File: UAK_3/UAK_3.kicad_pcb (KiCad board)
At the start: 2 copper layers, 100 x 90 mm, 63 parts, among them K1 Кнопка_FSMSM, K2 Кнопка_FSMSM, X1 Крепежное_отверстие_М3, X2 Крепежное_отверстие_М3, X3 Крепежное_отверстие_М3, X4 Крепежное_отверстие_М3

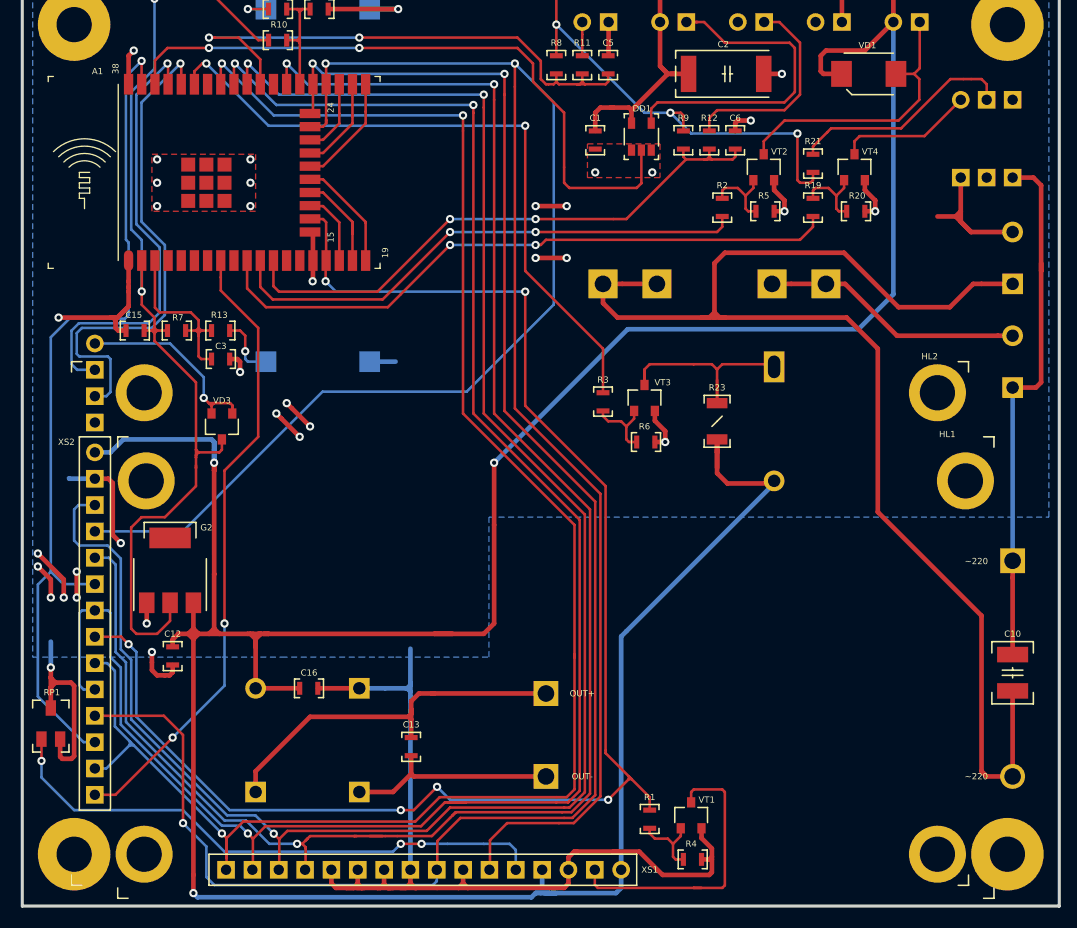
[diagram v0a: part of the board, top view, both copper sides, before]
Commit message: добавлены сопротивления: в управление ЖК и выход 220
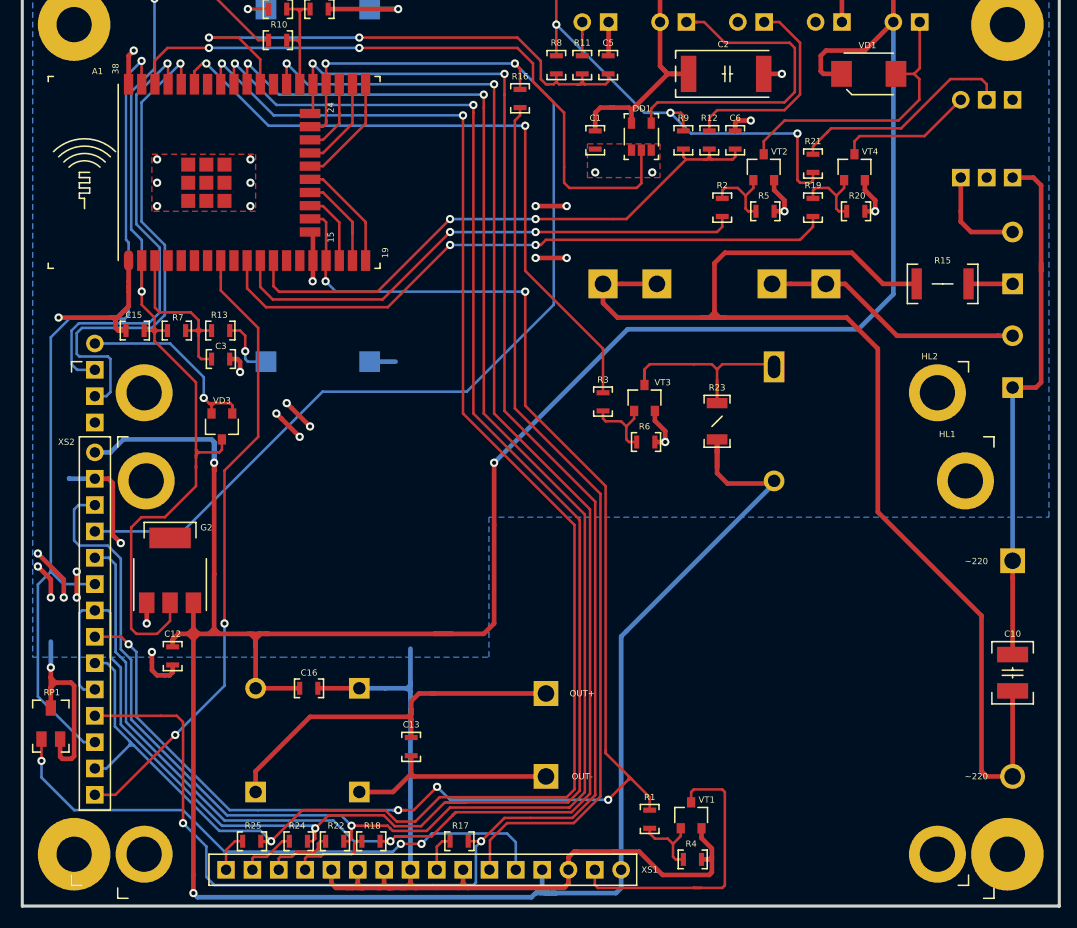
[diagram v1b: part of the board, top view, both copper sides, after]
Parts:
- added R15: Резистор_0,5Вт, N_RLC:Резистор_SMD_2010-0,5_Вт, F.Cu at (161.2, 80.0)
- added R16: Резистор_0,065Вт, N_RLC:Резистор_SMD_0603_0,065_Вт, F.Cu at (123.0, 63.0)
- added R17: Резистор_0,065Вт, N_RLC:Резистор_SMD_0603_0,065_Вт, F.Cu at (116.2, 133.8)
- added R18: Резистор_0,065Вт, N_RLC:Резистор_SMD_0603_0,065_Вт, F.Cu at (107.8, 133.8)
- added R22: Резистор_0,065Вт, N_RLC:Резистор_SMD_0603_0,065_Вт, F.Cu at (104.2, 133.8)
- added R24: Резистор_0,065Вт, N_RLC:Резистор_SMD_0603_0,065_Вт, F.Cu at (100.8, 133.8)
- added R25: Резистор_0,065Вт, N_RLC:Резистор_SMD_0603_0,065_Вт, F.Cu at (96.2, 133.8)
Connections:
- HL1 pad 11: /LCD_DATA_4 -> Net-(HL1-Pad11)
- HL1 pad 12: /LCD_DATA_5 -> Net-(HL1-Pad12)
- HL1 pad 13: /LCD_DATA_6 -> Net-(HL1-Pad13)
- HL1 pad 14: /LCD_DATA_7 -> Net-(HL1-Pad14)
- HL1 pad 4: /LCD_A0 -> Net-(HL1-Pad4)
- HL1 pad 6: /LCD_E -> Net-(HL1-Pad6)
- XT8 pad 2: /220_L_FU -> /220_L_OUT
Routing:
- net /LCD_A0: track 193.4 -> 106.8 mm
- net Net-(HL1-Pad4): track 0.00 -> 85.3 mm
- net /220_L_FU: track 131.9 -> 120.8 mm
- net Net-(HL1-Pad11): track 0.00 -> 7.70 mm
- net Net-(HL1-Pad12): track 0.00 -> 6.60 mm
- net Net-(HL1-Pad13): track 0.00 -> 5.34 mm
- net /220_N_OUT: track 14.2 -> 9.66 mm
- net /220_L_OUT: track 0.00 -> 4.25 mm
- net Net-(HL1-Pad14): track 0.00 -> 3.85 mm
- net Net-(HL1-Pad6): track 0.00 -> 3.72 mm
- net /LCD_DATA_4: track 169.3 -> 167.0 mm
- net /LCD_E: track 164.5 -> 166.3 mm, vias 3 -> 4
- net /LCD_DATA_5: track 177.0 -> 175.5 mm
- net Net-(HL1-Pad3): track 54.9 -> 56.1 mm
- net /LCD_LED: track 146.9 -> 148.1 mm
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
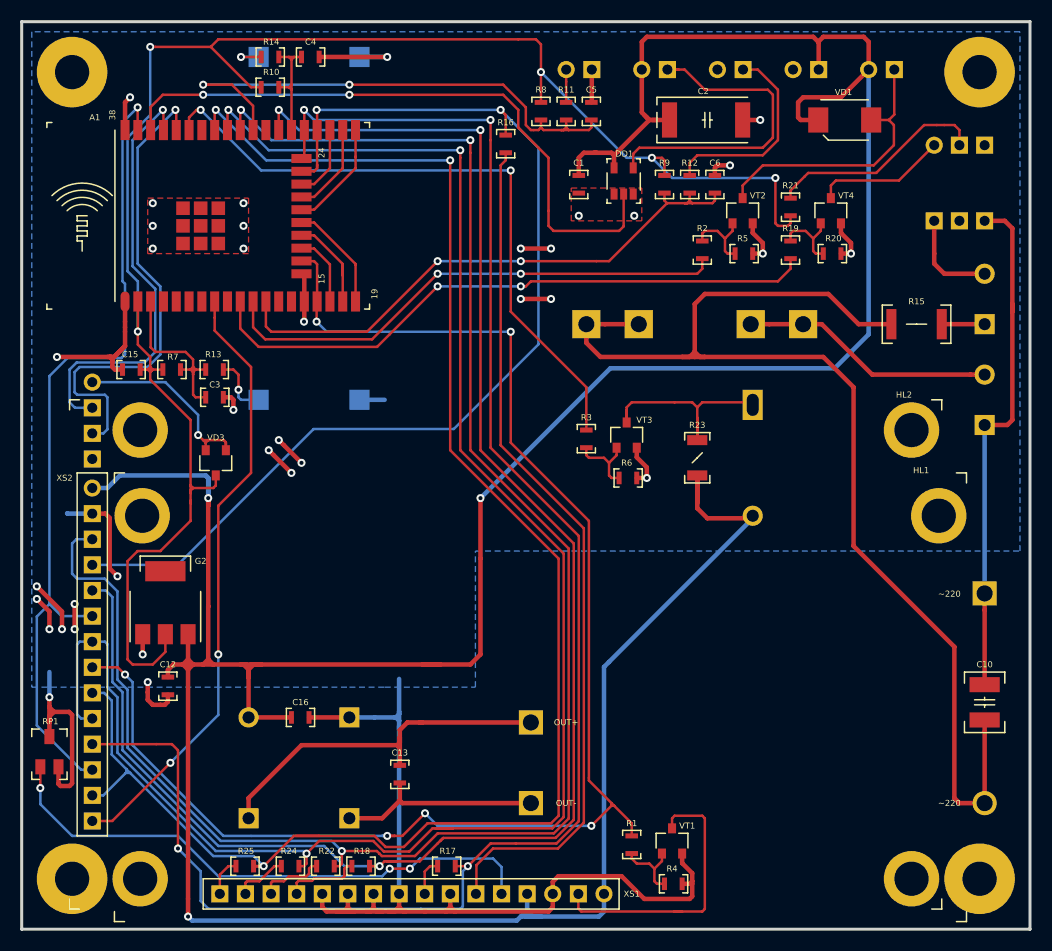
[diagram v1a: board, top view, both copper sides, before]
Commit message: заменены клеммники
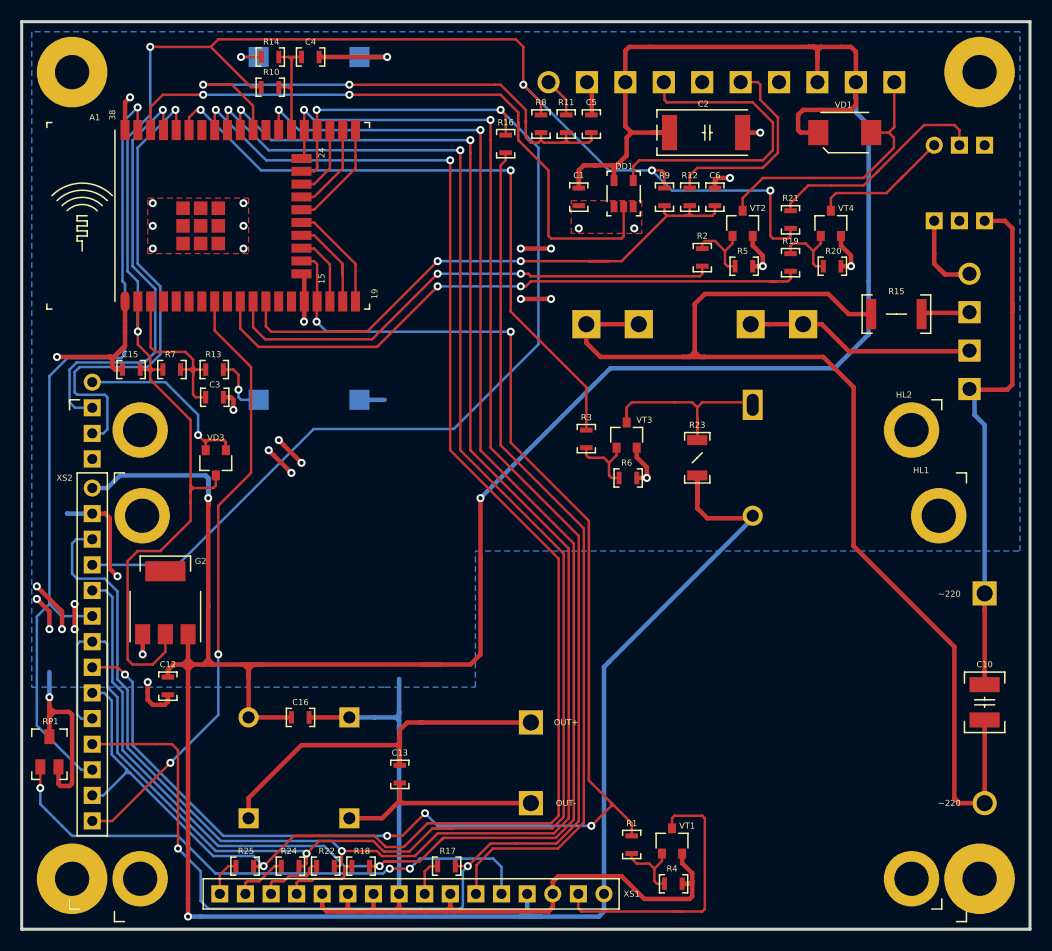
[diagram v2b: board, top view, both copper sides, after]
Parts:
- removed XT1, XT2, XT3, XT6, XT7: Клеммник_х2_308-021-14, N_X:Клеммник_х2_шаг2.54
- removed XT4, XT8: Клеммник_х2_KLS2-300-5.00-02P-2S, N_X:Клеммник_х2_шаг5
- added X5: Клеммник_х4, N_X:Клеммник_х4_шаг3,81_15EDGRC, B.Cu at (169.0, 75.0)
- added X6: Клеммник_х10, N_X:Клеммник_х10_шаг3,81_15EDGRC, B.Cu at (127.2, 56.0)
- moved D1 6.49 mm to (107.5, 66.8)
- moved R15 2.24 mm to (159.2, 79.0)
- moved C1 1.25 mm to (130.2, 66.5)
- moved C2 1.25 mm to (139.2, 61.0)
- moved C5 1.25 mm to (131.5, 59.2)
- moved C6 1.25 mm to (143.8, 66.5)
- moved DD1 1.25 mm to (133.8, 68.3)
- moved R11 1.25 mm to (129.0, 59.2)
- moved R12 1.25 mm to (141.2, 66.5)
- moved R19 1.25 mm to (151.2, 73.0)
- moved R20 1.25 mm to (154.5, 74.2)
- moved R21 1.25 mm to (151.2, 68.8)
- moved R5 1.25 mm to (145.8, 74.2)
- moved R8 1.25 mm to (126.5, 59.2)
- moved R9 1.25 mm to (138.8, 66.5)
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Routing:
- net /5V: track 367.5 -> 372.1 mm
- net /220_L_FU: track 120.8 -> 118.4 mm
- net /220_L: track 25.3 -> 23.3 mm
- net /3V3: track 174.1 -> 175.9 mm
- net /EXT_BUTTON: track 56.2 -> 57.6 mm
- net /220_N_OUT: track 9.66 -> 11.1 mm
- net /DOOR_SENSOR: track 53.1 -> 54.5 mm
- net /220_N: track 51.5 -> 52.7 mm
- net /220_L_OUT: track 4.25 -> 5.30 mm
- net Net-(DA1-Pad1): track 13.2 -> 14.2 mm
- net /LED_WS2812: track 63.7 -> 64.6 mm
- net Net-(DA1-Pad2): track 21.9 -> 22.8 mm
- net /DOOR_1: track 3.25 -> 3.97 mm
- net /LED_OUT: track 32.8 -> 32.1 mm
- net /D_OUT_1: track 27.6 -> 27.0 mm
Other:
- board text added: "BUTT LED"
- board text added: "EXT BUTTON"
- board text added: "LED WS2812"
- board text removed: "12V OUT"
- board text removed: "5V_OUT"
- board text removed: "BUTT_LED"
- board text removed: "EXT_BUTTON"
- board text removed: "LED_WS2812"

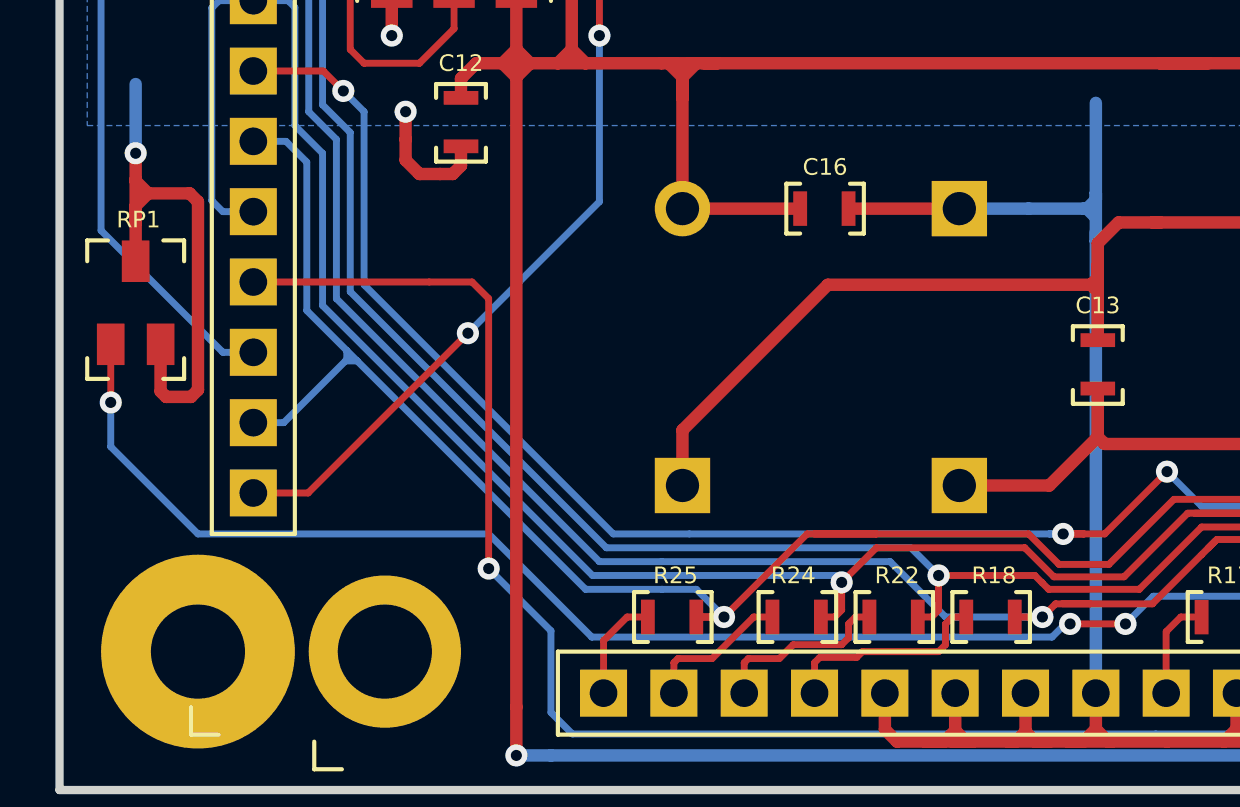
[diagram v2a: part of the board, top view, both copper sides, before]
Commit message: заменен потенциометр, начал формировать BOM
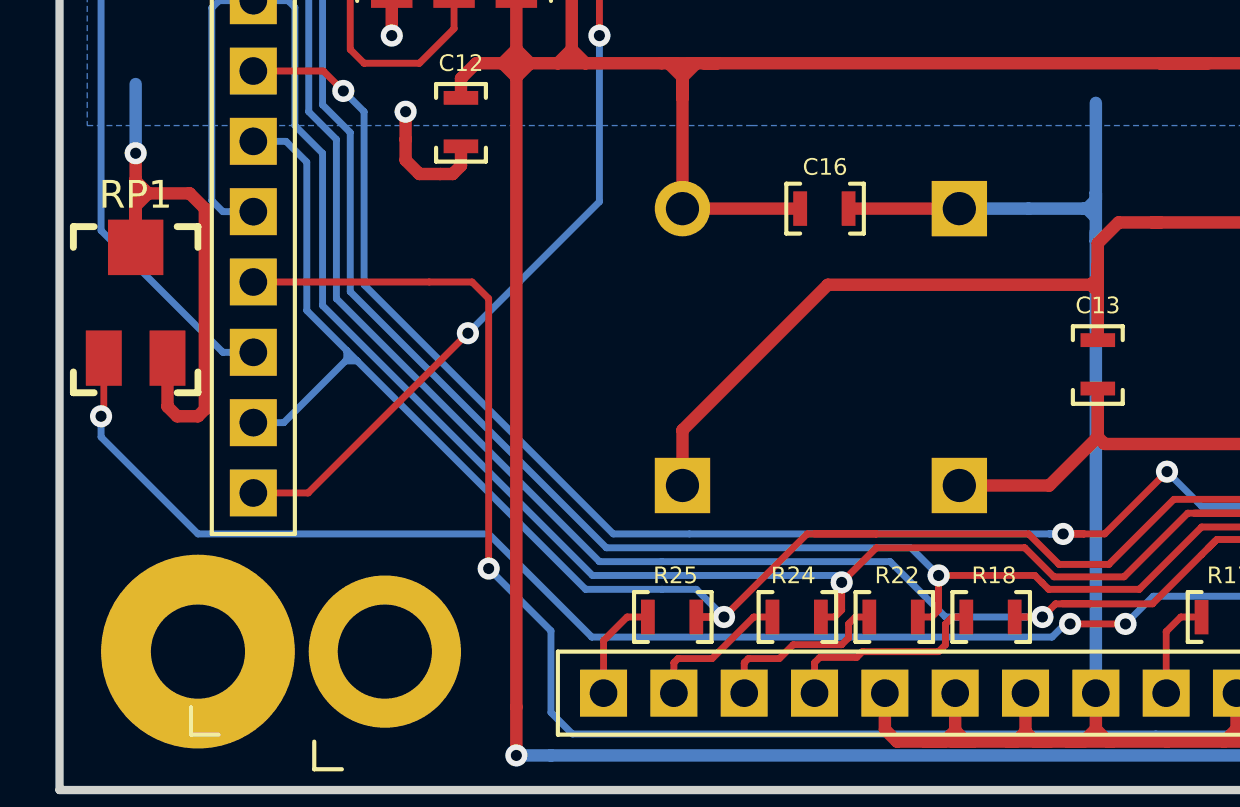
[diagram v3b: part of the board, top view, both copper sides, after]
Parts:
- RP1: footprint MOTOR_IMPORT_OTK:резистор_подстроечный_PVZ3A334 -> N_RLC:резистор_подстроечный_3314J-1
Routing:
- net /GND: track 214.0 -> 216.4 mm

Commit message: подготовлены файлы для заказа в JLCPCB
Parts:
- removed the R9 at (138.8, 66.5)
- added R20: Резистор_0,065Вт, N_RLC:Резистор_SMD_0603_0,065_Вт_pnp, F.Cu at (63.8, -72.6)
- A1: footprint N_A:ESP32_WROVER_or_WROOM32 -> N_A:ESP32_WROVER_or_WROOM32_pnp
- C1, C3, C4, C5, C6: footprint N_RLC:Конденсатор_SMD_0603 -> N_RLC:Конденсатор_SMD_0603_pnp
- C10: renamed from C13; footprint N_RLC:Конденсатор_SMD_0603 -> N_RLC:Конденсатор_SMD_0603_pnp
- C11: renamed from C16; footprint N_RLC:Конденсатор_SMD_0603 -> N_RLC:Конденсатор_SMD_0603_pnp
- C2: footprint MOTOR_RLC:Конденсатор_тантал_SMD_m7343 -> N_RLC:Конденсатор_тантал_SMD_m7343_pnp
- C7: renamed from C10; footprint N_RLC:Конденсатор_SMD_1210 -> N_RLC:Конденсатор_SMD_1210_pnp
- C8: renamed from C12; footprint N_RLC:Конденсатор_SMD_0603 -> N_RLC:Конденсатор_SMD_0603_pnp
- C9: renamed from C15; footprint N_RLC:Конденсатор_SMD_0603 -> N_RLC:Конденсатор_SMD_0603_pnp
- DD1: footprint N_G:Преобразователь_LM2703_SOT-23-5 -> N_G:SOT-23-5_pnp
- G2: footprint N_VD_HL:Транзистор_NPN_SOT223 -> N_VD_HL:Транзистор_NPN_SOT223_pnp
- R1: renamed from R19; footprint N_RLC:Резистор_SMD_0603_0,065_Вт -> N_RLC:Резистор_SMD_0603_0,065_Вт_pnp
- R10: renamed from R25; footprint N_RLC:Резистор_SMD_0603_0,065_Вт -> N_RLC:Резистор_SMD_0603_0,065_Вт_pnp
- R11: renamed from R1; footprint N_RLC:Резистор_SMD_0603_0,065_Вт -> N_RLC:Резистор_SMD_0603_0,065_Вт_pnp
- R12: renamed from R2; footprint N_RLC:Резистор_SMD_0603_0,065_Вт -> N_RLC:Резистор_SMD_0603_0,065_Вт_pnp
- R13: renamed from R3; footprint N_RLC:Резистор_SMD_0603_0,065_Вт -> N_RLC:Резистор_SMD_0603_0,065_Вт_pnp
- R14: renamed from R4; footprint N_RLC:Резистор_SMD_0603_0,065_Вт -> N_RLC:Резистор_SMD_0603_0,065_Вт_pnp
- R15: renamed from R5; footprint N_RLC:Резистор_SMD_0603_0,065_Вт -> N_RLC:Резистор_SMD_0603_0,065_Вт_pnp
- R16: renamed from R6; footprint N_RLC:Резистор_SMD_0603_0,065_Вт -> N_RLC:Резистор_SMD_0603_0,065_Вт_pnp
- R17: renamed from R23; footprint N_RLC:Резистор_SMD_1206-0,25_Вт -> N_RLC:Резистор_SMD_1206-0,25_Вт_pnp
- R18: renamed from R7; footprint N_RLC:Резистор_SMD_0603_0,065_Вт -> N_RLC:Резистор_SMD_0603_0,065_Вт_pnp
- R19: renamed from R8; footprint N_RLC:Резистор_SMD_0603_0,065_Вт -> N_RLC:Резистор_SMD_0603_0,065_Вт_pnp
- R2: renamed from R20; footprint N_RLC:Резистор_SMD_0603_0,065_Вт -> N_RLC:Резистор_SMD_0603_0,065_Вт_pnp
- R21: renamed from R10; footprint N_RLC:Резистор_SMD_0603_0,065_Вт -> N_RLC:Резистор_SMD_0603_0,065_Вт_pnp
- R22: renamed from R11; footprint N_RLC:Резистор_SMD_0603_0,065_Вт -> N_RLC:Резистор_SMD_0603_0,065_Вт_pnp
- R23: renamed from R12; footprint N_RLC:Резистор_SMD_0603_0,065_Вт -> N_RLC:Резистор_SMD_0603_0,065_Вт_pnp
- R24: renamed from R13; footprint N_RLC:Резистор_SMD_0603_0,065_Вт -> N_RLC:Резистор_SMD_0603_0,065_Вт_pnp
- R25: renamed from R14; footprint N_RLC:Резистор_SMD_0603_0,065_Вт -> N_RLC:Резистор_SMD_0603_0,065_Вт_pnp
- R3: renamed from R21; footprint N_RLC:Резистор_SMD_0603_0,065_Вт -> N_RLC:Резистор_SMD_0603_0,065_Вт_pnp
- R4: renamed from R15; footprint N_RLC:Резистор_SMD_2010-0,5_Вт -> N_RLC:Резистор_SMD_2010-0,5_Вт_pnp
- R5: renamed from R16; footprint N_RLC:Резистор_SMD_0603_0,065_Вт -> N_RLC:Резистор_SMD_0603_0,065_Вт_pnp
- R6: renamed from R17; footprint N_RLC:Резистор_SMD_0603_0,065_Вт -> N_RLC:Резистор_SMD_0603_0,065_Вт_pnp
- R7: renamed from R18; footprint N_RLC:Резистор_SMD_0603_0,065_Вт -> N_RLC:Резистор_SMD_0603_0,065_Вт_pnp
- R8: renamed from R22; footprint N_RLC:Резистор_SMD_0603_0,065_Вт -> N_RLC:Резистор_SMD_0603_0,065_Вт_pnp
- R9: renamed from R24; footprint N_RLC:Резистор_SMD_0603_0,065_Вт -> N_RLC:Резистор_SMD_0603_0,065_Вт_pnp
- RP1: footprint N_RLC:резистор_подстроечный_3314J-1 -> N_RLC:резистор_подстроечный_3314J-1_pnp
- VD1: footprint N_VD_HL:Диод_SMB -> N_VD_HL:Диод_SMB_pnp
- VD2: renamed from VD3; footprint MOTOR_VD_VT_HL:Корпус_КТ-46 -> N_DD:Корпус_КТ-46_pnp
- VT1: renamed from VT4; footprint MOTOR_VD_VT_HL:Корпус_КТ-46 -> N_DD:Корпус_КТ-46_pnp
- VT2: renamed from VT1; footprint MOTOR_VD_VT_HL:Корпус_КТ-46 -> N_DD:Корпус_КТ-46_pnp
- VT3: renamed from VT2; footprint MOTOR_VD_VT_HL:Корпус_КТ-46 -> N_DD:Корпус_КТ-46_pnp
- VT4: renamed from VT3; footprint MOTOR_VD_VT_HL:Корпус_КТ-46 -> N_DD:Корпус_КТ-46_pnp
- moved A1 162.5 mm to (19.2, -70.8)
- moved C7 160.4 mm to (95.5, -22.5)
- moved R17 160.4 mm to (67.0, -46.8)
- moved VD1 160.0 mm to (81.6, -79.0), turned to 0 degrees
- moved R11 159.6 mm to (60.5, -8.38)
- moved R13 159.6 mm to (56.0, -48.6)
- moved R5 159.6 mm to (48.0, -77.9)
- moved DD1 159.4 mm to (59.7, -72.8), turned to 90 degrees
- moved C9 159.2 mm to (10.9, -55.5)
- moved R24 159.2 mm to (19.1, -55.5)
- moved D1 158.8 mm to (66.7, -67.8)
- moved D2 158.8 mm to (32.5, -73.2)
- moved DA1 158.8 mm to (90.5, -77.8)
- moved G1 158.8 mm to (95.5, -12.5)
- moved HA1 158.8 mm to (72.5, -46.5)
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- renumbered D2 to D1, D1 to D2, HL2 to HL1, HL1 to HL2, L2 to L1, X5 to X1, X6 to X2, X1 to X3, X2 to X4, X3 to X5, X4 to X6
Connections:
- VD1 pad 1: /D_OUT_1 -> /5V
- VD1 pad 2: /5V -> /D_OUT_1
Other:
- board text added: "UAK.3A.N5"
- board text removed: "UAK.2B.MN"
